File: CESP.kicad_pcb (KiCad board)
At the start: 2 copper layers, 55.9 x 44.7 mm, 9 parts

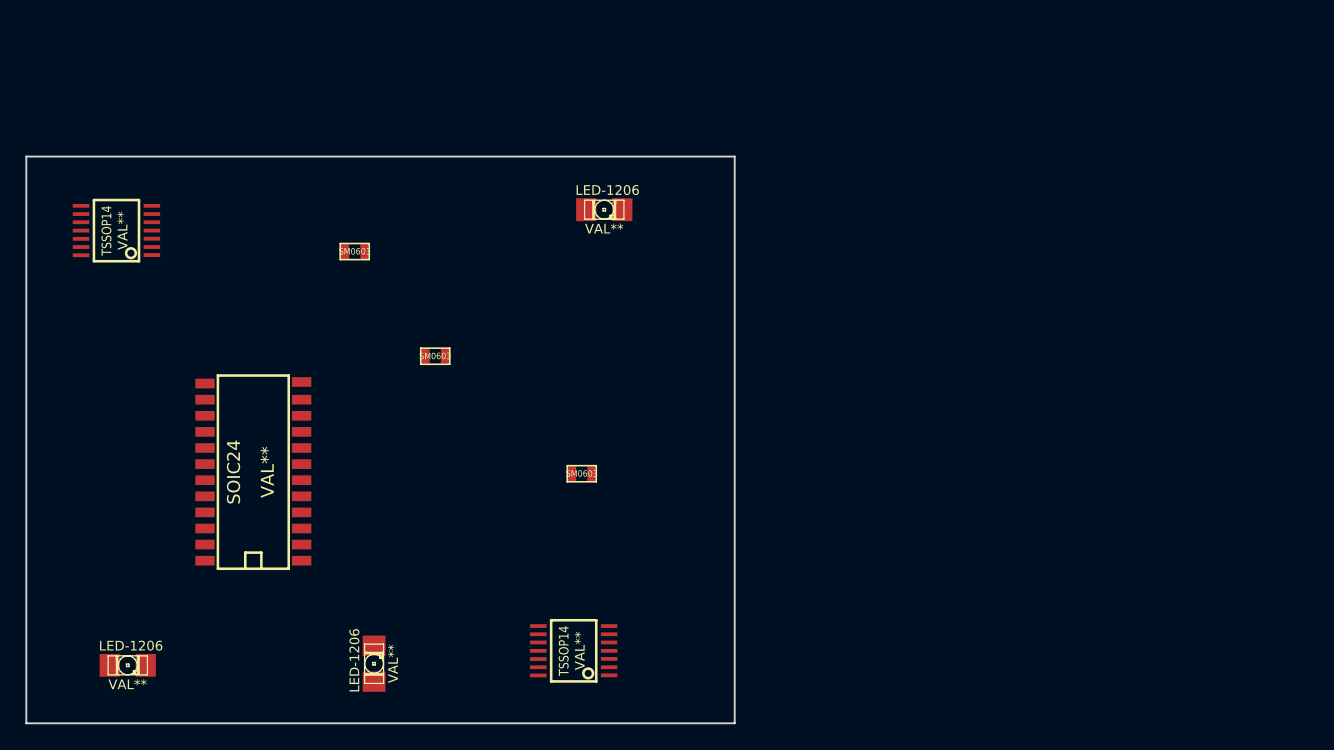
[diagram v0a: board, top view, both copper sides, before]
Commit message: Added Large Footprint
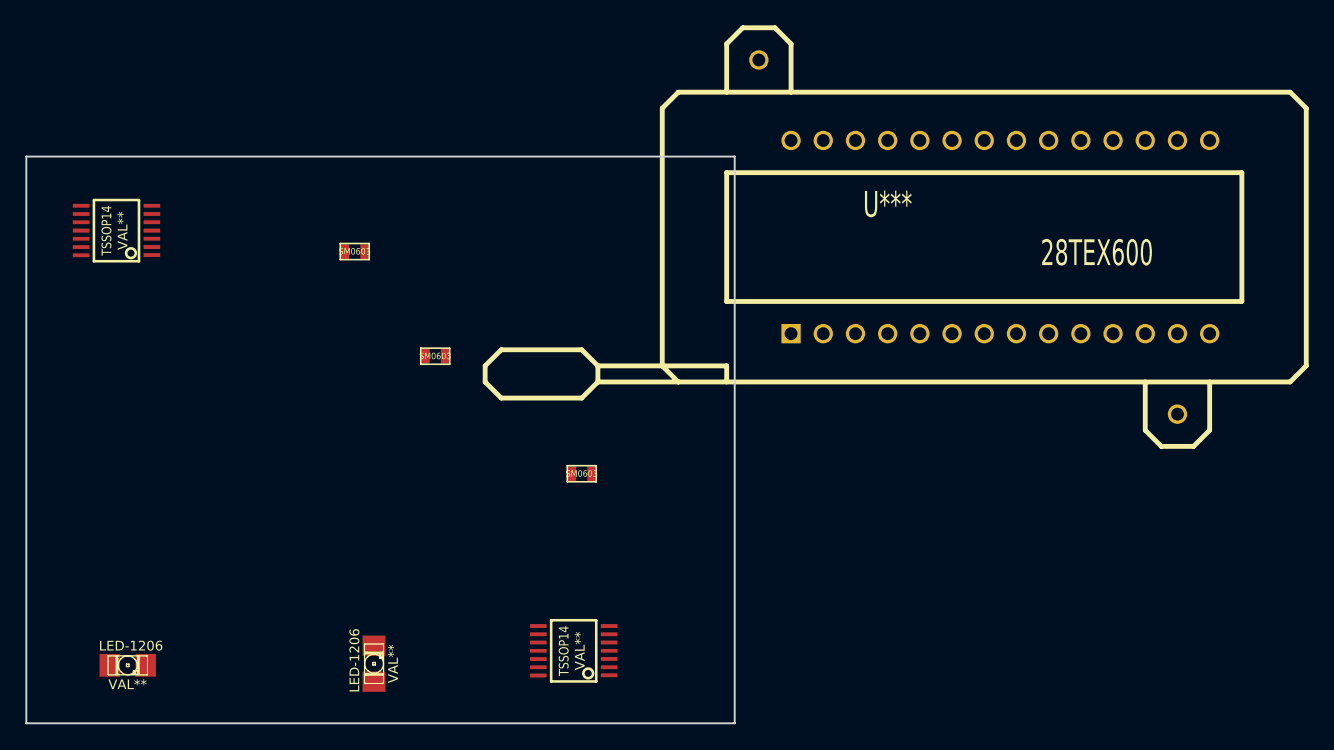
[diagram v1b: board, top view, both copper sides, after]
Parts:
- removed the LED-1206 at (201.5, 99.9)
- removed SOIC24: VAL**, SOIC24
- added U***: 28TEX600, 28tex600, F.Cu at (232.8, 102.1)
